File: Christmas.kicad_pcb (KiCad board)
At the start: 2 copper layers, 61.2 x 78.7 mm, 13 parts

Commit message: Started wiring V0.1
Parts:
- moved S1 0.67 mm to (125.9, 72.9)
- moved D2 0.47 mm to (110.3, 33.0)
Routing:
- net Net-(D1-A): track 0.00 -> 150.3 mm
- net Net-(BT1--): track 0.00 -> 138.4 mm
- net Net-(R1-Pad1): track 0.00 -> 33.6 mm
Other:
- board text added: "06-12-2023"
- board text added: "Liefs, Casper Tak"
- board text removed: "Liefs, Casper Tak 06-12-2023"

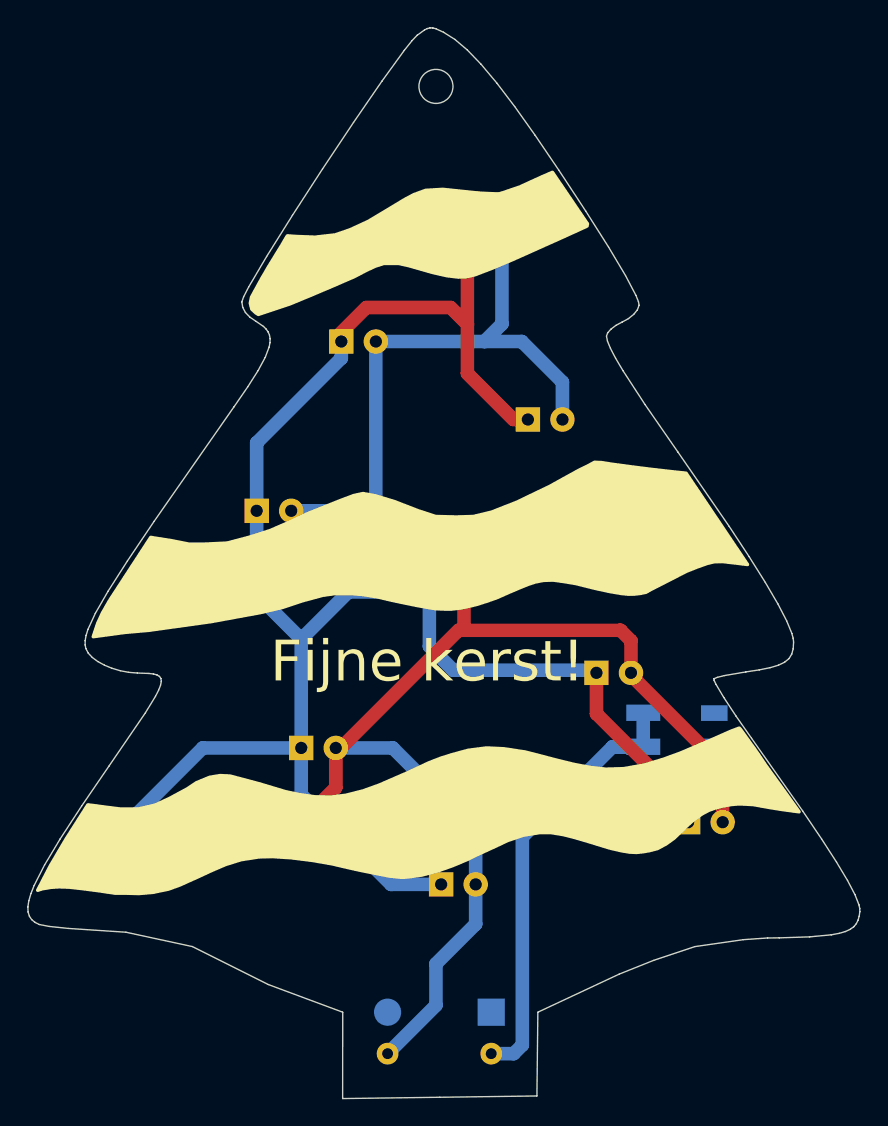
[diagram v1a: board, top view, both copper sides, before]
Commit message: Improved wiring aesthetics
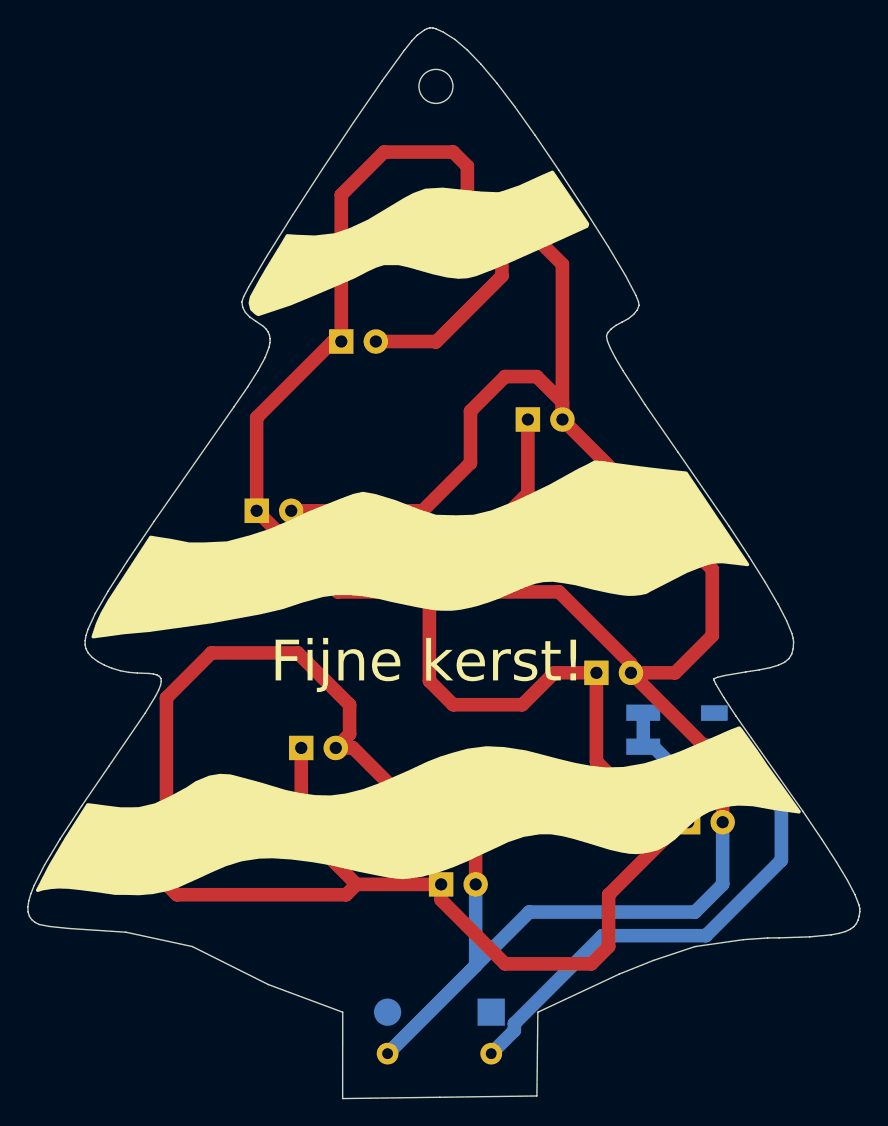
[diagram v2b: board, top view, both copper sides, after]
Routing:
- net Net-(D1-A): track 150.3 -> 216.5 mm
- net Net-(BT1--): track 138.4 -> 170.4 mm
- net Net-(R1-Pad1): track 33.6 -> 46.3 mm

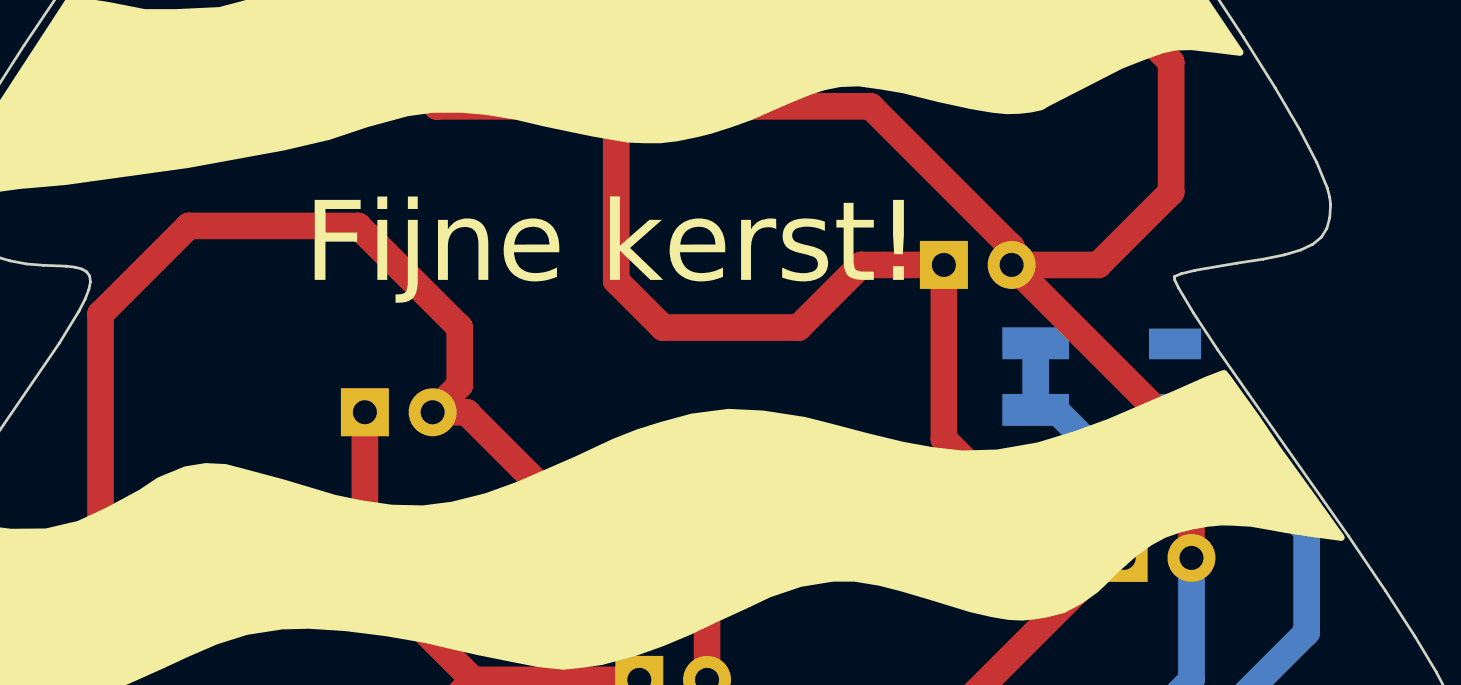
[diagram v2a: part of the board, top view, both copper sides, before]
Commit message: Minor silkscreen improvements
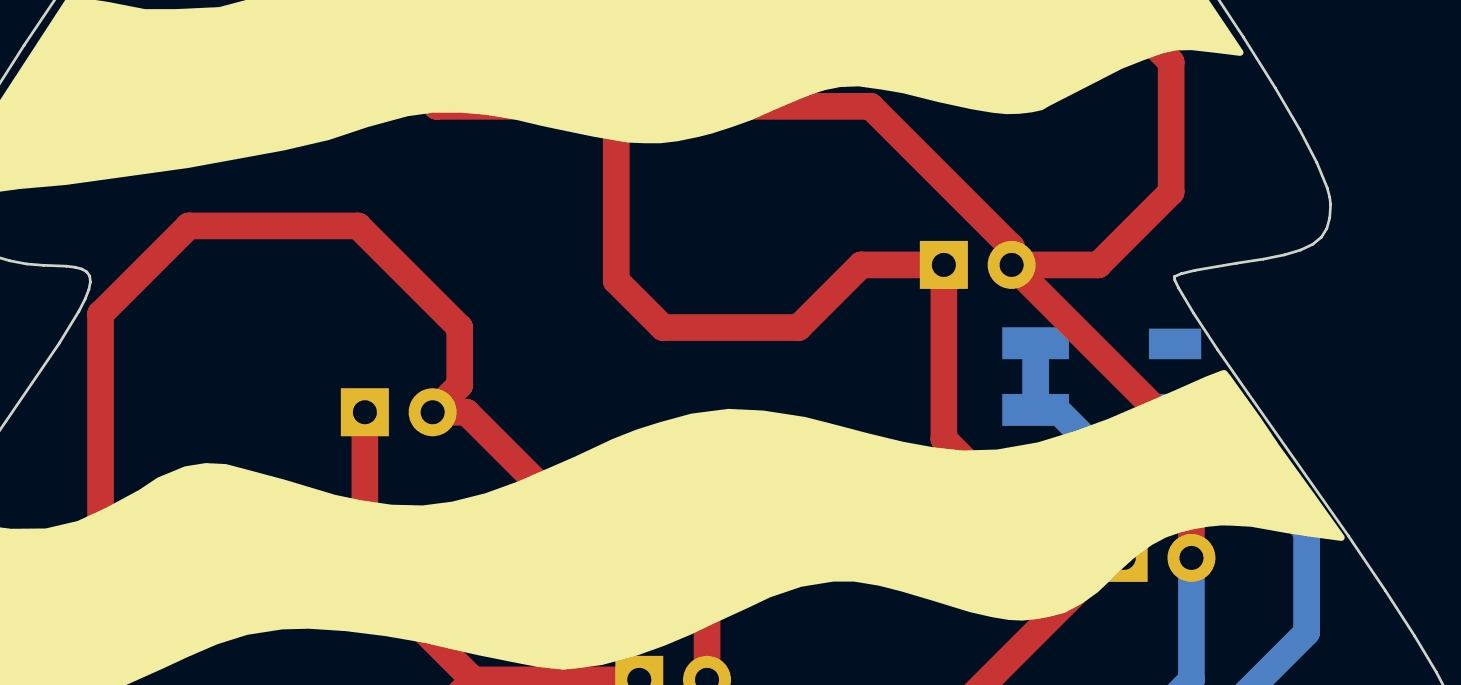
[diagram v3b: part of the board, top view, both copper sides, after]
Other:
- board text added: "ON"
- board text removed: "Fijne kerst!"

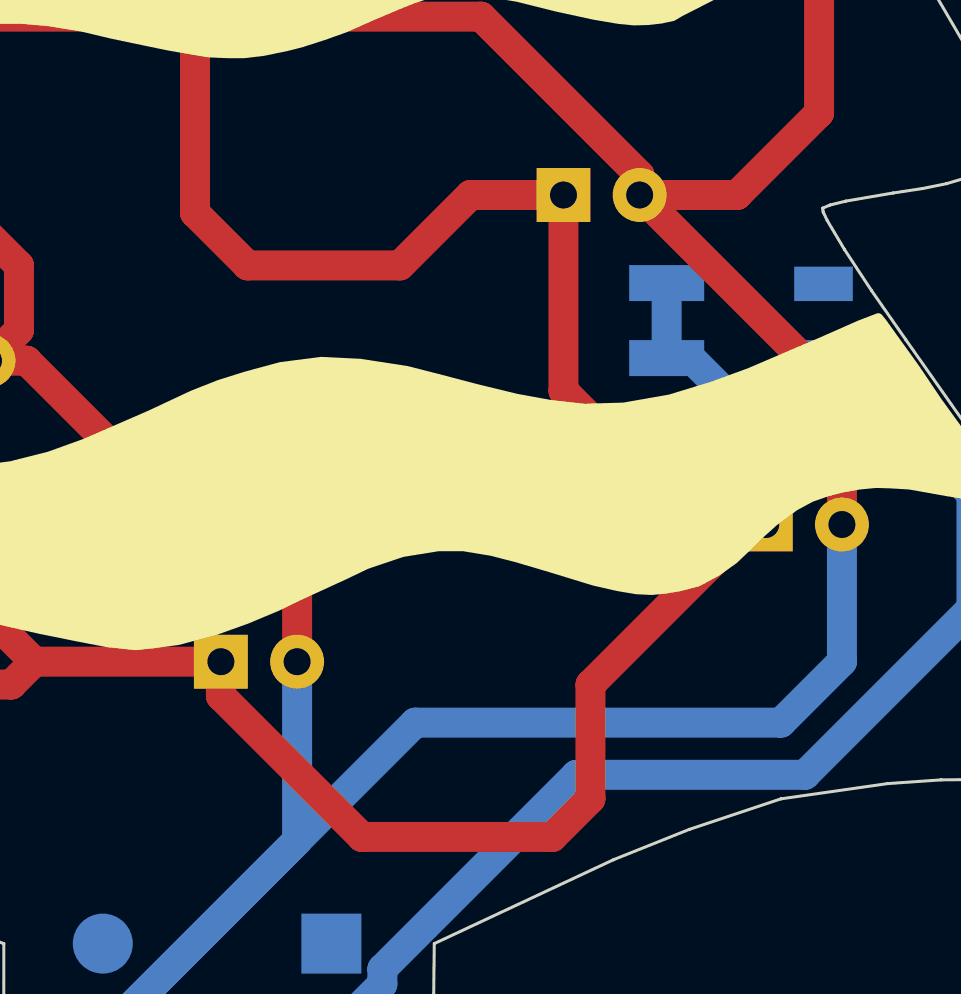
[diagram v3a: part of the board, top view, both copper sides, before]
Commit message: Minor routing improvements
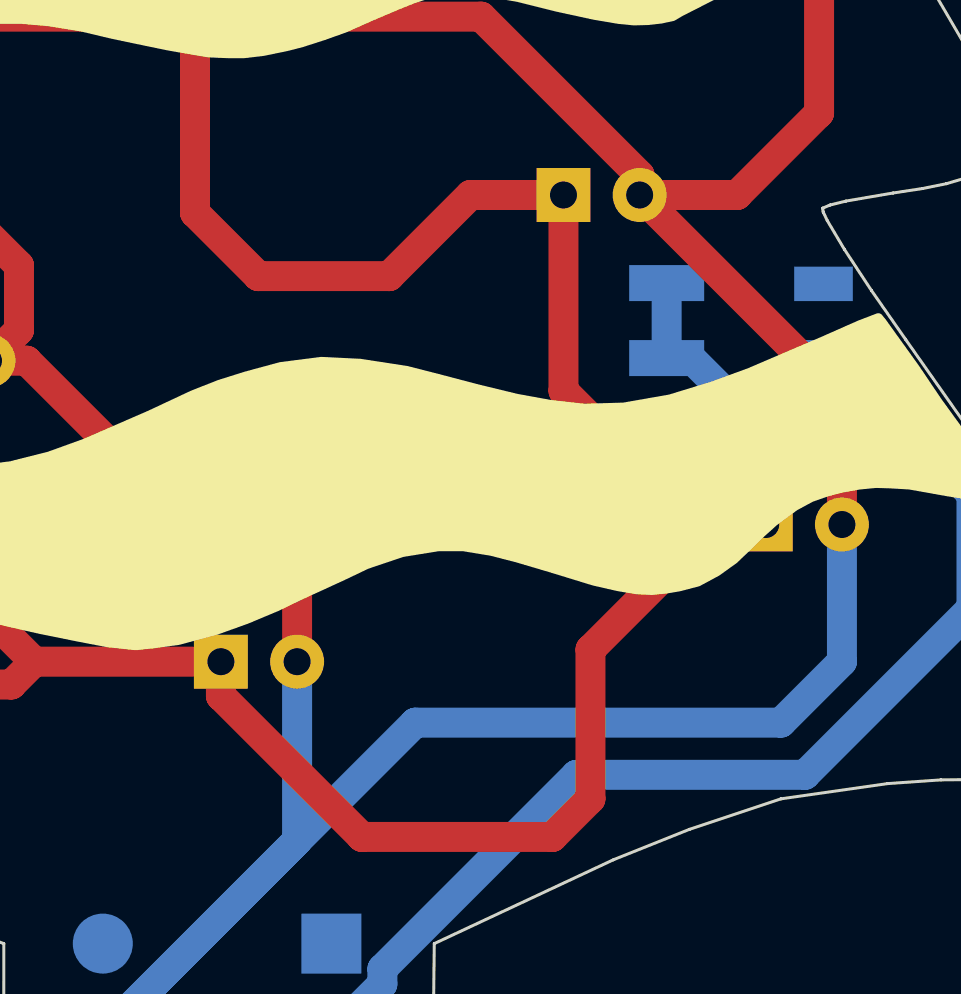
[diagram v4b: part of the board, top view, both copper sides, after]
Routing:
- net Net-(BT1--): track 170.4 -> 171.3 mm
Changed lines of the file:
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@@
   )
   (segment (start 85.598 80.518) (end 88.9 83.82) (width 1) (layer "F.Cu") (net 2))
-  (segment (start 108.331 83.058) (end 108.331 84.201) (width 1) (layer "F.Cu") (net 2))
-  (segment (start 107.4674 61.5569) (end 107.4674 68.0974) (width 1) (layer "F.Cu") (net 2))
+  (segment (start 109.5756 70.2056) (end 113.9444 70.2056) (width 1) (layer "F.Cu") (net 2))
   (segment (start 94.7674 48.7426) (end 94.7674 55.5879) (width 1) (layer "F.Cu") (net 2))
-  (segment (start 113.03 88.9) (end 119.38 88.9) (width 1) (layer "F.Cu") (net 2))
+  (segment (start 120.65 82.6516) (end 124.8156 78.486) (width 1) (layer "F.Cu") (net 2))
   (segment (start 100.3681 43.1419) (end 94.7674 48.7426) (width 1) (layer "F.Cu") (net 2))
   (segment (start 85.593 80.518) (end 85.598 80.518) (width 1) (layer "F.Cu") (net 2))
-  (segment (start 107.4674 68.0974) (end 109.22 69.85) (width 1) (layer "F.Cu") (net 2))
+  (segment (start 108.331 84.201) (end 113.03 88.9) (width 1) (layer "F.Cu") (net 2))
   (segment (start 114.7094 48.877) (end 114.7094 54.3149) (width 1) (layer "F.Cu") (net 2))
   (segment (start 100.9904 43.1419) (end 100.3681 43.1419) (width 1) (layer "F.Cu") (net 2))
-  (segment (start 108.331 84.201) (end 113.03 88.9) (width 1) (layer "F.Cu") (net 2))
   (segment (start 98.044 73.025) (end 98.044 78.994) (width 1) (layer "F.Cu") (net 2))
-  (segment (start 116.648 67.502) (end 119.7494 67.502) (width 1) (layer "F.Cu") (net 2))
   (segment (start 101.346 83.82) (end 102.108 83.058) (width 1) (layer "F.Cu") (net 2))
-  (segment (start 120.65 87.63) (end 120.65 83.82) (width 1) (layer "F.Cu") (net 2))
-  (segment (start 114.3 69.85) (end 116.648 67.502) (width 1) (layer "F.Cu") (net 2))
   (segment (start 119.7494 74.0294) (end 119.7494 67.502) (width 1) (layer "F.Cu") (net 2))
   (segment (start 110.2614 30.2514) (end 109.22 29.21) (width 1) (layer "F.Cu") (net 2))
+  (segment (start 107.4674 68.0974) (end 109.5756 70.2056) (width 1) (layer "F.Cu") (net 2))
+  (segment (start 119.38 88.9) (end 120.65 87.63) (width 1) (layer "F.Cu") (net 2))
   (segment (start 126.492 78.486) (end 124.206 78.486) (width 1) (layer "F.Cu") (net 2))
   (segment (start 88.9 83.82) (end 101.346 83.82) (width 1) (layer "F.Cu") (net 2))
+  (segment (start 124.8156 78.486) (end 126.492 78.486) (width 1) (layer "F.Cu") (net 2))
   (segment (start 114.7094 54.3149) (end 107.4674 61.5569) (width 1) (layer "F.Cu") (net 2))
   (segment (start 100.9904 32.3596) (end 100.9904 43.1419) (width 1) (layer "F.Cu") (net 2))
   (segment (start 107.4674 61.5569) (end 100.7364 61.5569) (width 1) (layer "F.Cu") (net 2))
-  (segment (start 109.22 69.85) (end 114.3 69.85) (width 1) (layer "F.Cu") (net 2))
-  (segment (start 119.38 88.9) (end 120.65 87.63) (width 1) (layer "F.Cu") (net 2))
+  (segment (start 120.65 87.63) (end 120.65 82.6516) (width 1) (layer "F.Cu") (net 2))
+  (segment (start 113.03 88.9) (end 119.38 88.9) (width 1) (layer "F.Cu") (net 2))
+  (segment (start 108.331 83.058) (end 108.331 84.201) (width 1) (layer "F.Cu") (net 2))
+  (segment (start 113.9444 70.2056) (end 116.648 67.502) (width 1) (layer "F.Cu") (net 2))
+  (segment (start 107.4674 61.5569) (end 107.4674 68.0974) (width 1) (layer "F.Cu") (net 2))
+  (segment (start 116.648 67.502) (end 119.7494 67.502) (width 1) (layer "F.Cu") (net 2))
   (segment (start 98.044 78.994) (end 102.108 83.058) (width 1) (layer "F.Cu") (net 2))
   (segment (start 110.2614 33.02) (end 110.2614 30.2514) (width 1) (layer "F.Cu") (net 2))
-  (segment (start 125.984 78.486) (end 126.492 78.486) (width 1) (layer "F.Cu") (net 2))
   (segment (start 109.22 29.21) (end 104.14 29.21) (width 1) (layer "F.Cu") (net 2))
-  (segment (start 120.65 83.82) (end 125.984 78.486) (width 1) (layer "F.Cu") (net 2))
   (segment (start 104.14 29.21) (end 100.9904 32.3596) (width 1) (layer "F.Cu") (net 2))
   (segment (start 102.108 83.058) (end 108.331 83.058) (width 1) (layer "F.Cu") (net 2))

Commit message: final improvements to V0.1 of pcb
-improved silkscreen
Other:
- board text added: "V0.1"

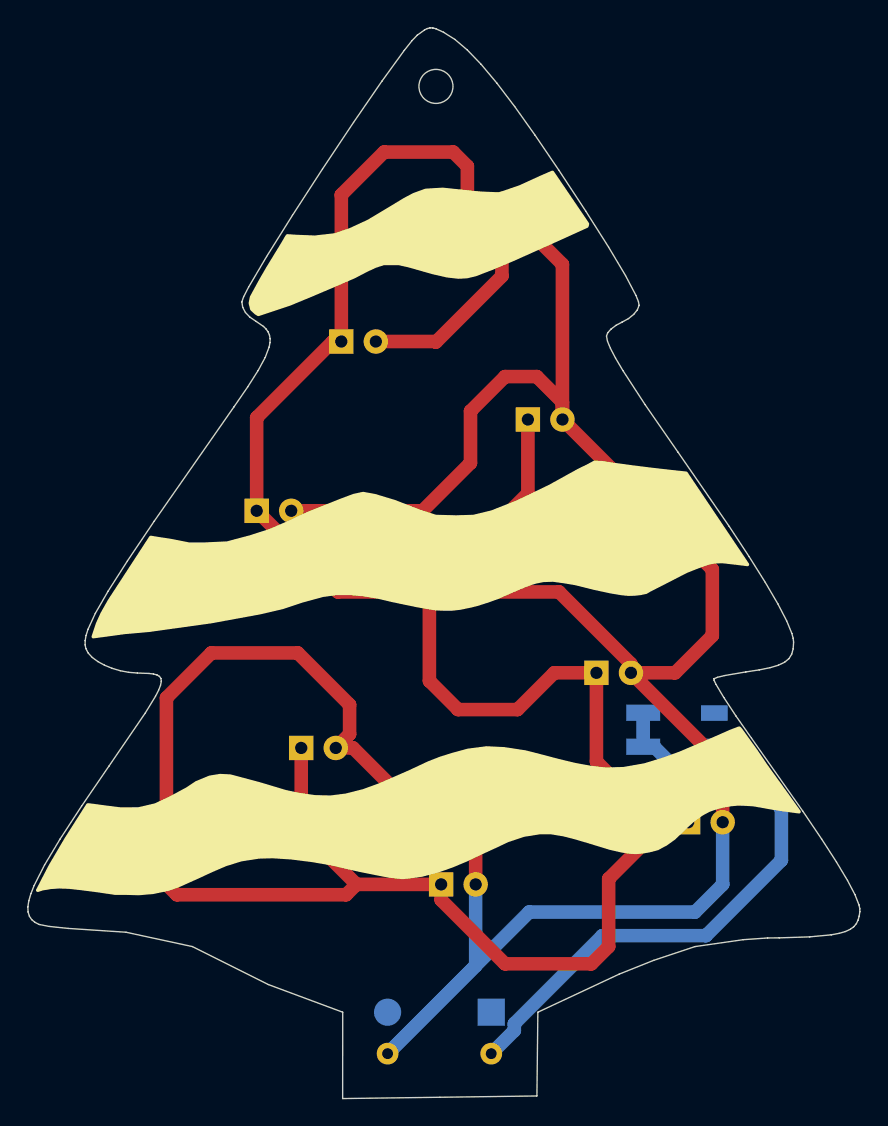
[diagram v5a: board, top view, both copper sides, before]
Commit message: V0.2 of board added
- added missing power traces from battery box pads
- improved aesthetics of tracks
- improved silkscreen text thickness
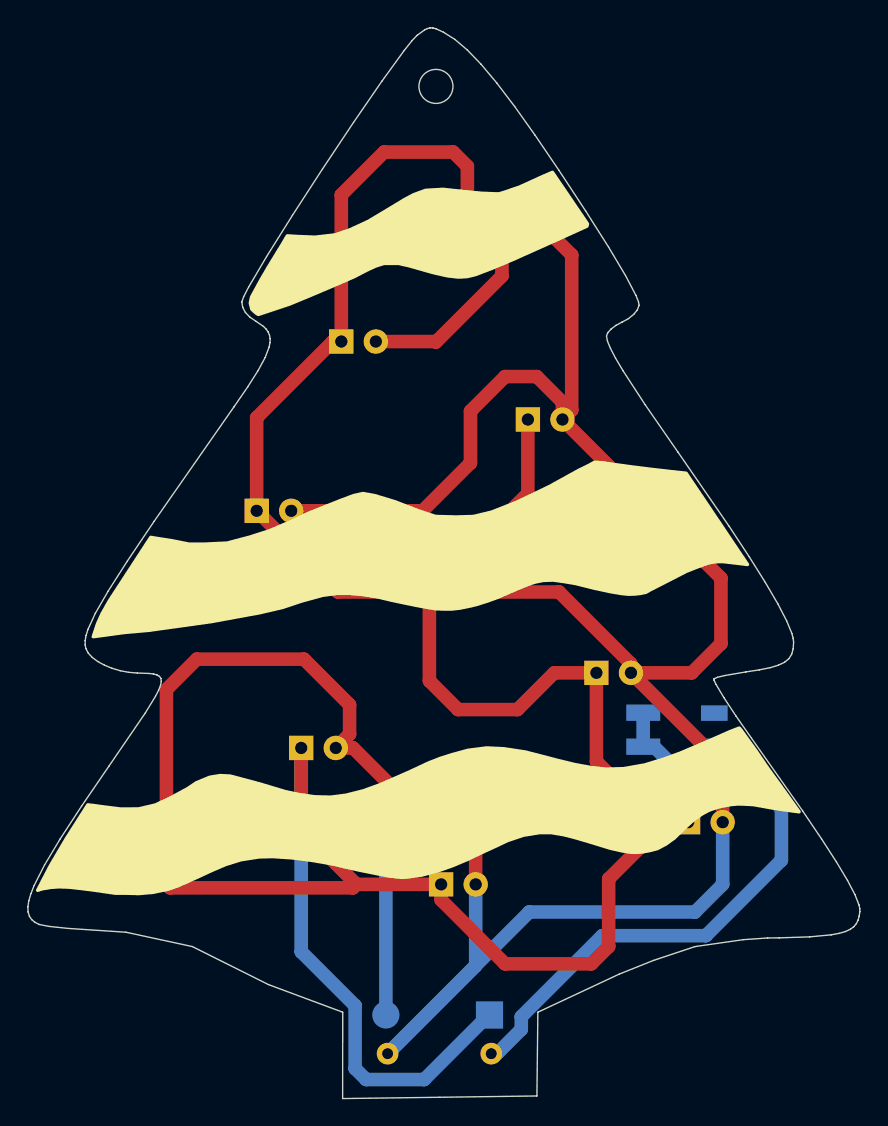
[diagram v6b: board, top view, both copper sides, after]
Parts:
- moved BT1 0.24 mm to (114.4, 87.6)
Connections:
- BT1 pad 1: (no net) -> Net-(BT1--)
- BT1 pad 2: (no net) -> Net-(BT1-+)
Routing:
- net Net-(BT1--): track 171.3 -> 208.4 mm
- net Net-(BT1-+): track 0.00 -> 33.8 mm
- net Net-(D1-A): track 216.5 -> 219.1 mm
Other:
- board text added: "18-12-2023"
- board text added: "V0.2"
- board text removed: "06-12-2023"
- board text removed: "V0.1"
